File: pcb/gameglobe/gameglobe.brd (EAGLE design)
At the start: 98.4 x 49.5 mm, 16 parts

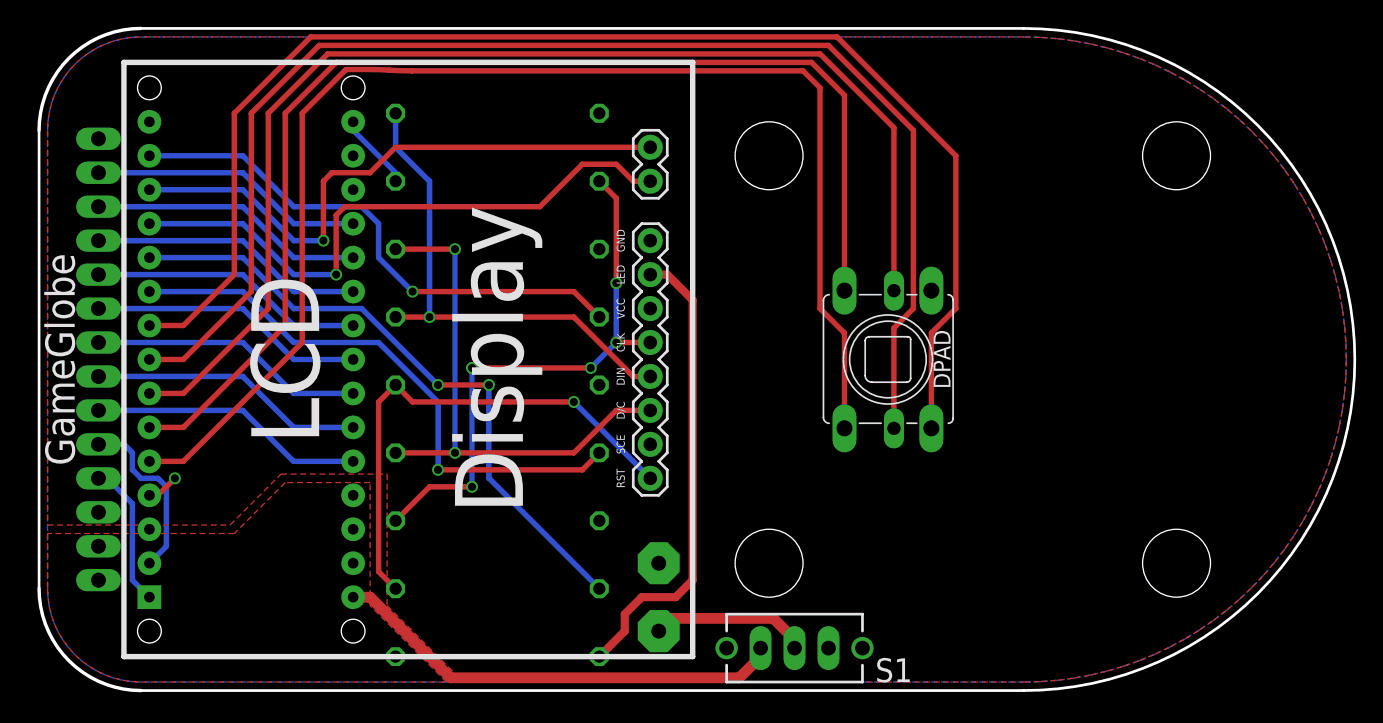
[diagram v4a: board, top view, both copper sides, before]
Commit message: Improved power plane layout, also improved silkscreen, updated mockup image with new pcb renders
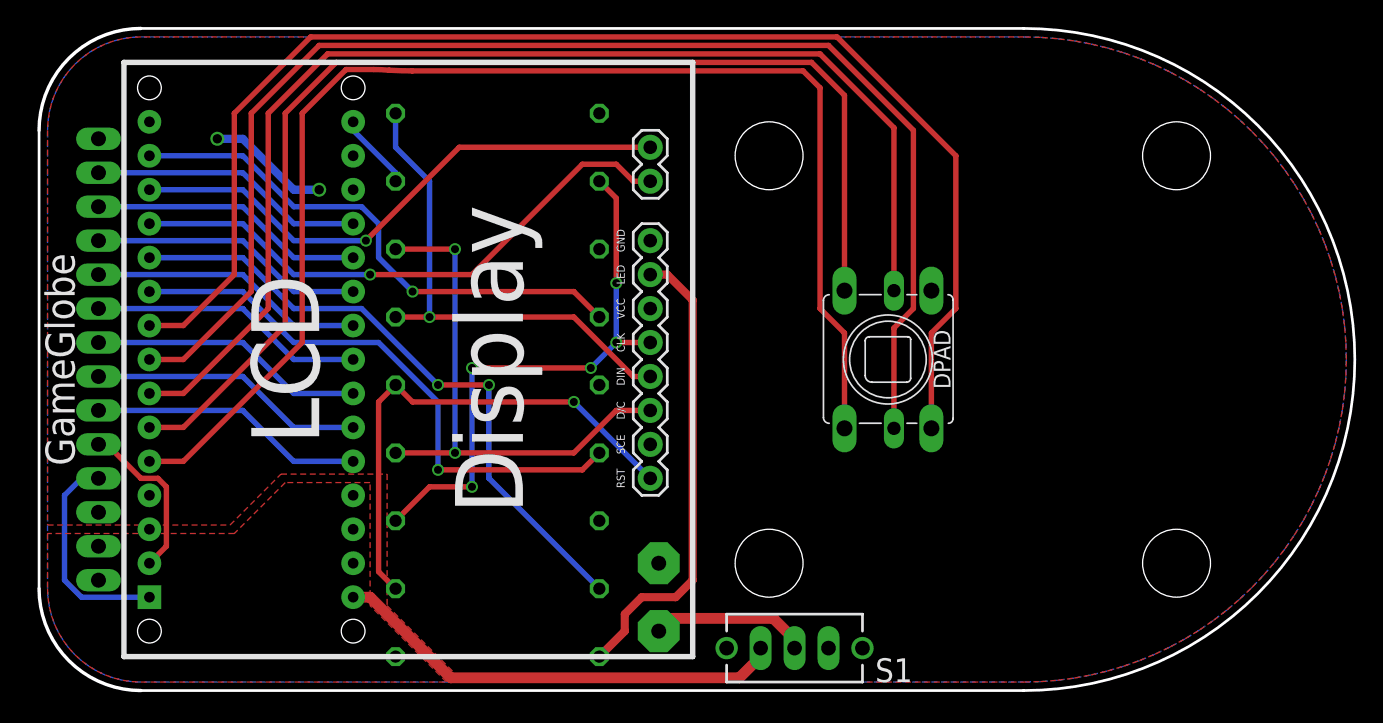
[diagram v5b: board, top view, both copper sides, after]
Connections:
- net N$11 renamed A0
- net N$12 renamed A1
- net N$13 renamed A2
- net N$14 renamed A3
- net N$15 renamed A4
- net N$16 renamed A5
- net N$17 renamed A6
- net N$18 renamed A7
- net N$7 renamed TX
- net N$8 renamed RX
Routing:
- net 3V3: track 0.00 -> 9.20 mm, vias 0 -> 2
- net TX: track 10.8 -> 16.3 mm
- net N$4: track 45.6 -> 43.0 mm
- net N$10: track 44.5 -> 41.9 mm
- net GND: track 2.43 -> 0.00 mm, vias 1 -> 0
- net RX: track 13.4 -> 12.6 mm
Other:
- board text added: "3V3"
- board text added: "5V"
- board text added: "A0"
- board text added: "A1"
- board text added: "A2"
- board text added: "A3"
- board text added: "A4"
- board text added: "A5"
- board text added: "A6"
- board text added: "A7"
- board text added: "Game"
- board text added: "Globe"
- board text added: "RX"
- board text added: "TX"

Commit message: Increased pad sizes, swapped DPAD left/right pins for better routing, improved silkscreen text
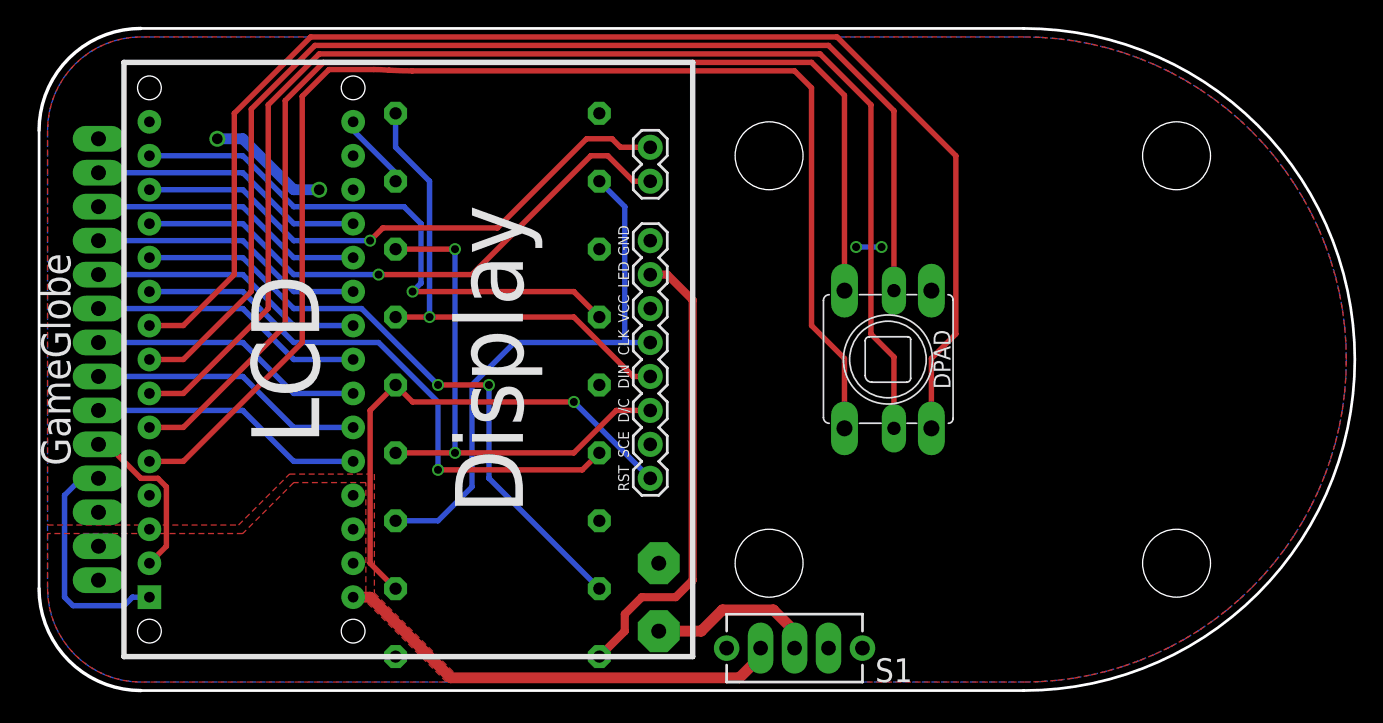
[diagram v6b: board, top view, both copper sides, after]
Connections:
- net DPAD_LEFT: now also ARDUINO_NANO.D4; no longer ARDUINO_NANO.D5
- net DPAD_RIGHT: now also ARDUINO_NANO.D5; no longer ARDUINO_NANO.D4
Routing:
- net N$2: track 40.1 -> 42.5 mm
- net 3V3: track 9.20 -> 11.1 mm, vias 2 -> 4
- net TX: track 16.3 -> 17.6 mm
- net N$6: track 11.8 -> 12.7 mm
- net DPAD_CENTER: track 88.2 -> 88.8 mm
- net N$4: track 43.0 -> 43.5 mm
- net LCD_RST: track 38.2 -> 38.8 mm
- net N$10: track 41.9 -> 42.5 mm
- net LCD_CLK: track 42.4 -> 41.9 mm, vias 5 -> 0

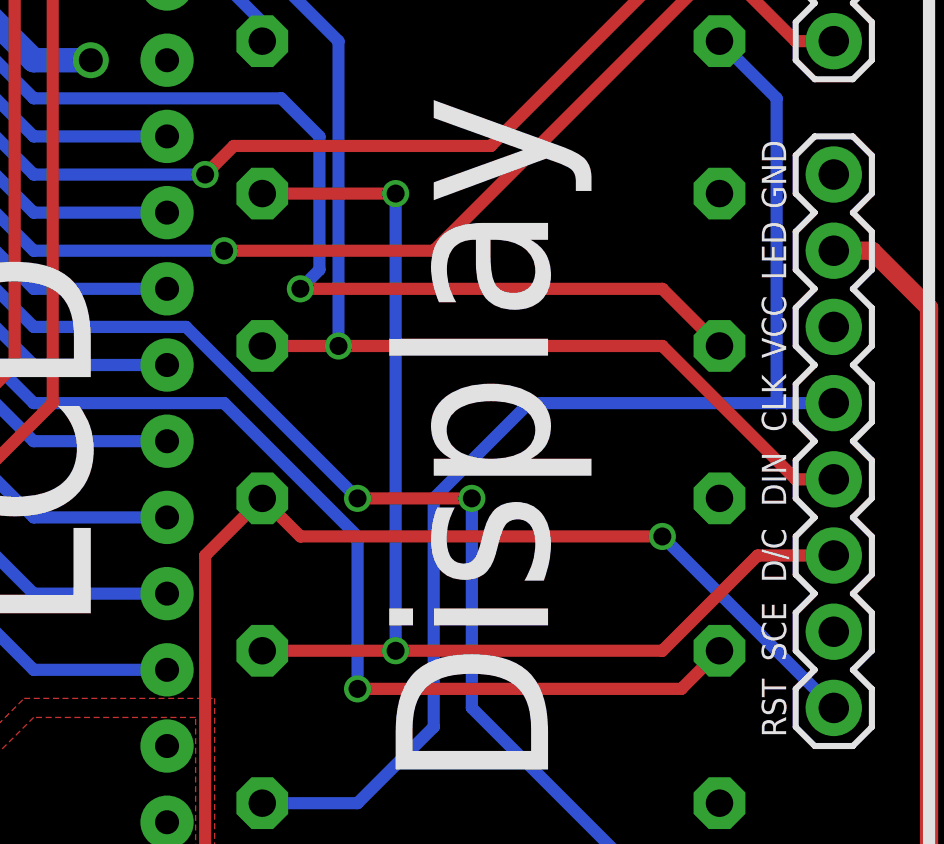
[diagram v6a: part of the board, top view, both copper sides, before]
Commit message: Resistor renaming and related silkscreen fixes
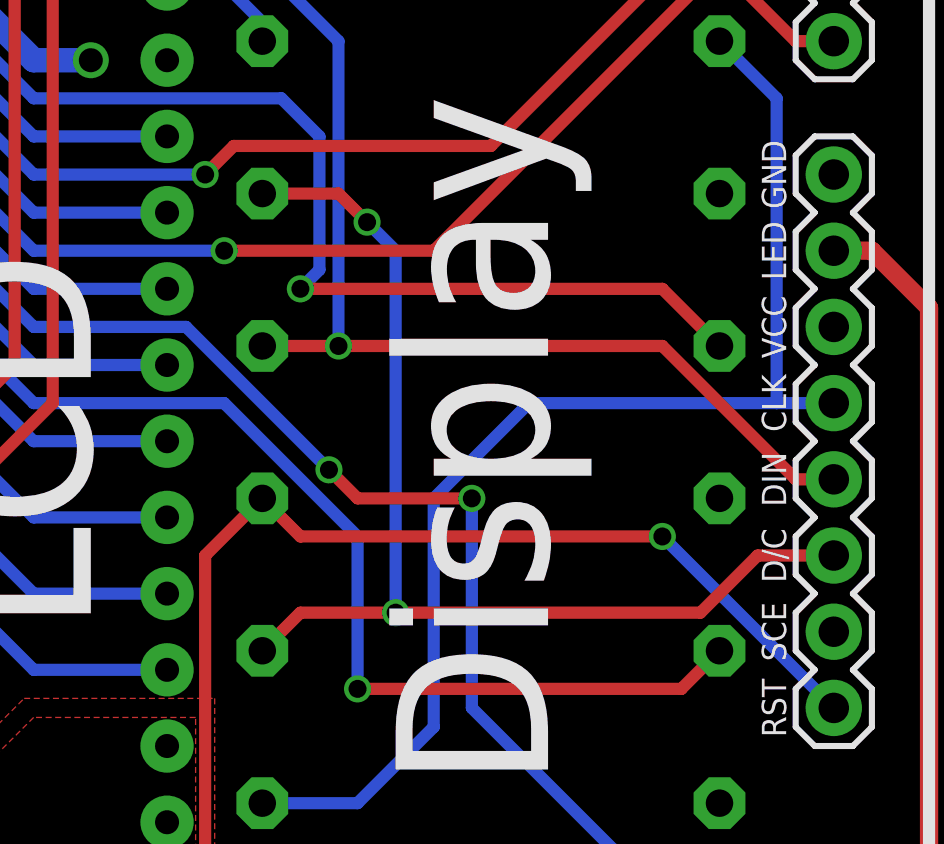
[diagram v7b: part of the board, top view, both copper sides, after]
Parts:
- removed R15: 20k, resistor:0411/15
- added R8: 10k, resistor:0411/15
- R5: value 10k -> 20k
- moved R5 15.2 mm to (34.3, 23.5)
- renumbered R10 to R6, R11 to R2, R12 to R4, R13 to R3, R14 to R7, R16 to R9
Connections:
- net GND: now also R5.1; no longer R15.1
- net LCD_CLK: now also R8.1; no longer R5.1
- net LCD_RST: now also R5.2; no longer R15.2
- net N$1: now also R8.2; no longer R5.2
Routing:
- net LCD_DC: track 40.1 -> 37.7 mm

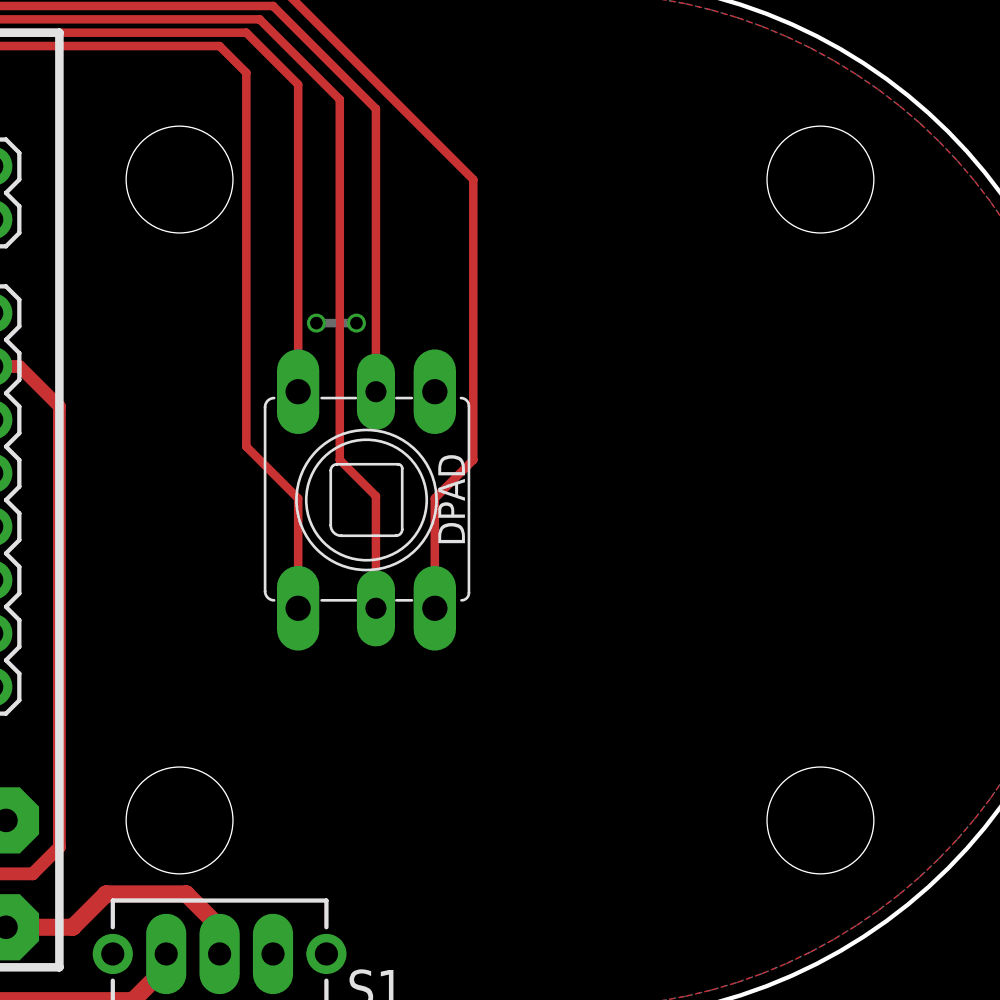
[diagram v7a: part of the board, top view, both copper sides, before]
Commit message: New generic silkscreen design
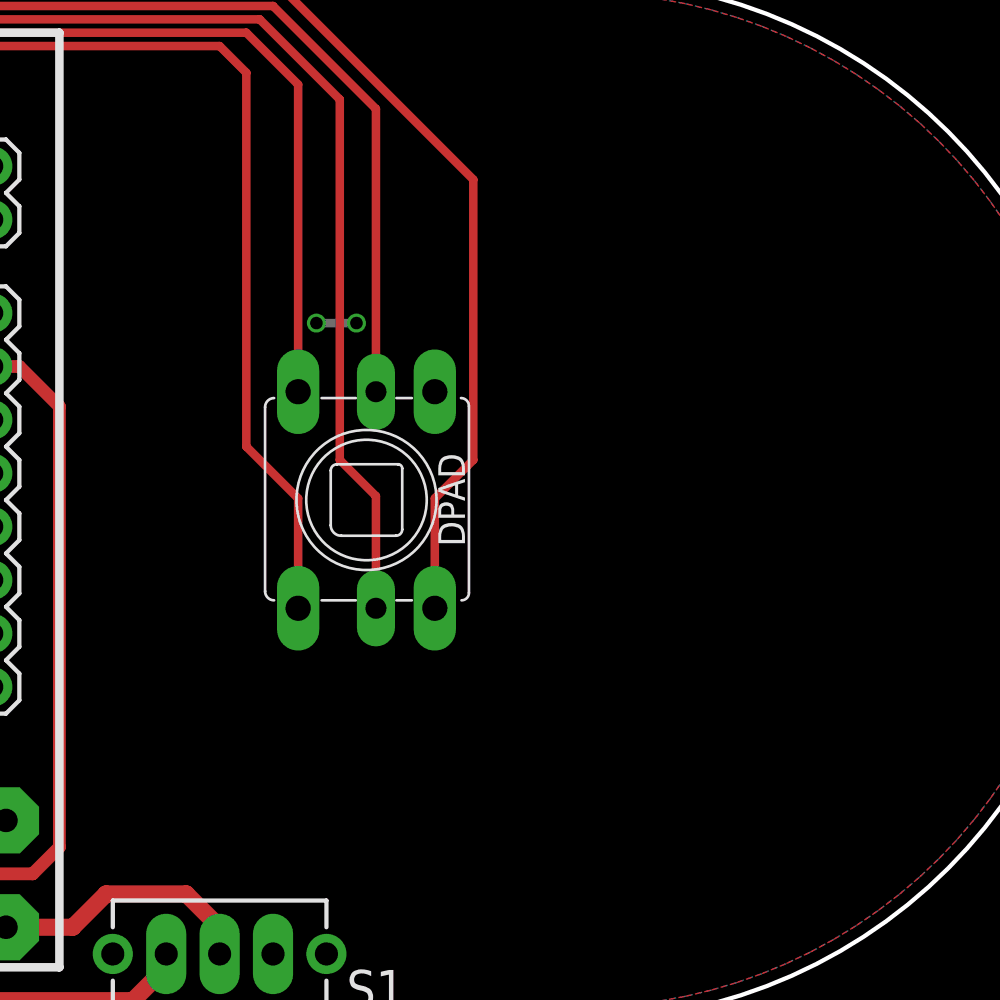
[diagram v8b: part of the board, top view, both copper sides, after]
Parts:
- R2, R4, R6, R8: value 10k -> 1k
- R3, R5, R7, R9: value 20k -> 2k
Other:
- board text removed: "Scouts 2, Globetrotters Scouting de Meridiaan Almere, NL"
